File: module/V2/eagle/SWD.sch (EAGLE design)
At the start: 238 parts, among them J2 KLDX-0202-A, SW1 MF-SW-TACT-6MM, SW2 MF-SW-TACT-6MM, U1 P8X32A-Q44, U10 SN74LV4066APWR, U11 SN74LV4066APWR, U12 SN74LV4066APWR, U13 SN74LV4066APWR, U14 SN74LV4066APWR, U15 SN74LV4066APWR, U16 SN74LV4066APWR, U17 SN74LV4066APWR, U18 SN74LV4066APWR, U19 SN74LV4066APWR, U2 CAT24C512WI-GT3, U20 SN74LV4066APWR, U21 SN74LV4066APWR, U22 SN74LV4066APWR, U23 SN74LV4066APWR, U24 SSM6J507NU,LF, U25 SSM6J507NU,LF, U26 SSM6J507NU,LF, U27 SSM6J507NU,LF, U3 FT230XQ-R, U4 SN74LV4066APWR, U5 SN74LV4066APWR, U6 SN74LV4066APWR, U7 SN74LV4066APWR, U8 SN74LV4066APWR, U9 SN74LV4066APWR, X1 ABMM-6.000MHZ-B2-T

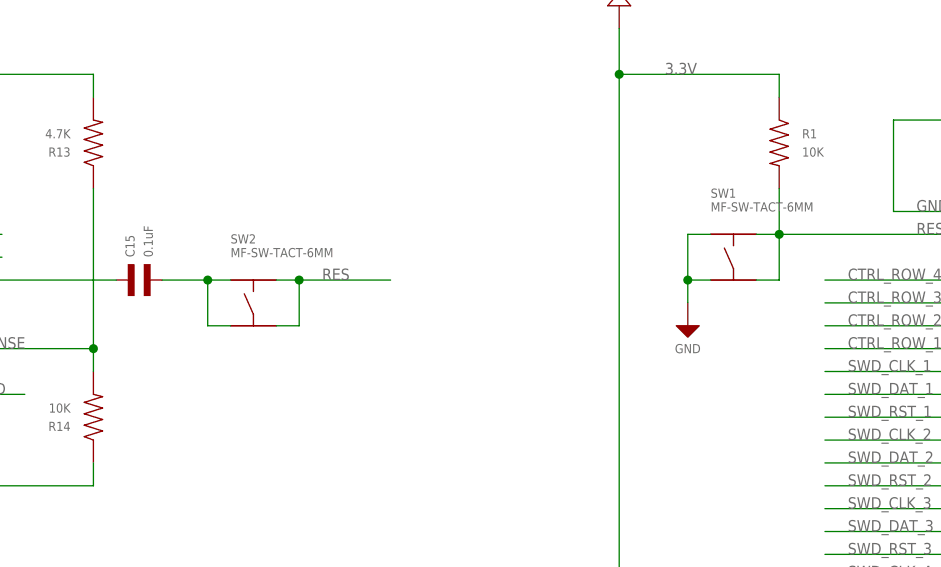
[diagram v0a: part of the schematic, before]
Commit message: Fixed wire errors
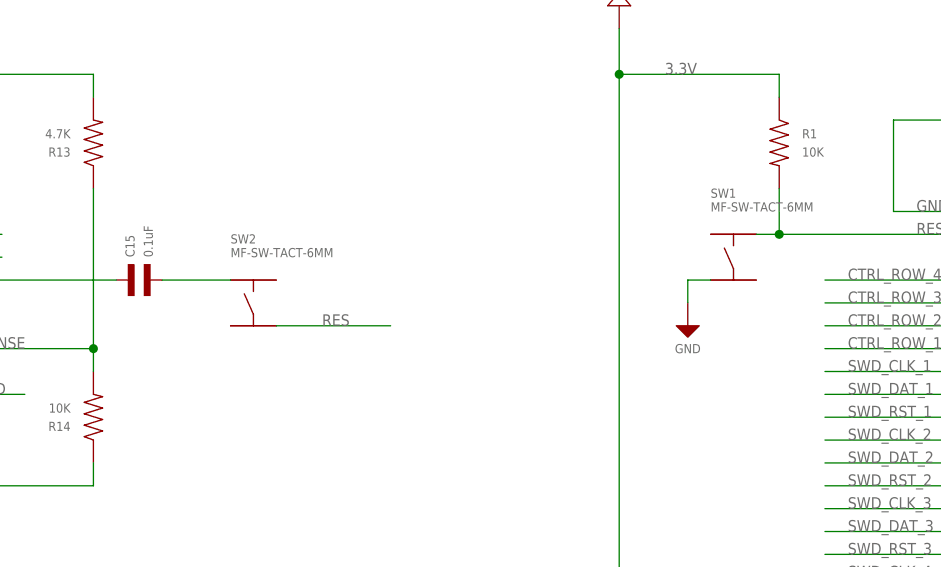
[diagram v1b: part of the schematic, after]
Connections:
- net GND: no longer SW1.P$1
- net N$18: no longer SW2.P$3
- net RES: no longer SW1.P$4, SW2.P$2
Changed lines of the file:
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@@
 <junction x="15.24" y="109.22"/>
 <label x="30.48" y="109.22" size="1.27" layer="95" font="vector"/>
-<pinref part="SW1" gate="G$1" pin="P$4"/>
-<wire x1="12.7" y1="104.14" x2="15.24" y2="104.14" width="0.1524" layer="91"/>
-<wire x1="15.24" y1="104.14" x2="15.24" y2="109.22" width="0.1524" layer="91"/>
-</segment>
-<segment>
-<pinref part="SW2" gate="G$1" pin="P$2"/>
-<wire x1="-40.64" y1="104.14" x2="-38.1" y2="104.14" width="0.1524" layer="91"/>
-<label x="-35.56" y="104.14" size="1.27" layer="95" font="vector"/>
+</segment>
+<segment>
+<label x="-35.56" y="99.06" size="1.27" layer="95" font="vector"/>
 <pinref part="SW2" gate="G$1" pin="P$4"/>
-<wire x1="-38.1" y1="104.14" x2="-27.94" y2="104.14" width="0.1524" layer="91"/>
-<wire x1="-40.64" y1="99.06" x2="-38.1" y2="99.06" width="0.1524" layer="91"/>
-<wire x1="-38.1" y1="99.06" x2="-38.1" y2="104.14" width="0.1524" layer="91"/>
-<junction x="-38.1" y="104.14"/>
+<wire x1="-40.64" y1="99.06" x2="-27.94" y2="99.06" width="0.1524" layer="91"/>
 </segment>
 </net>
@@
 <wire x1="7.62" y1="104.14" x2="5.08" y2="104.14" width="0.1524" layer="91"/>
 <wire x1="5.08" y1="104.14" x2="5.08" y2="101.6" width="0.1524" layer="91"/>
-<pinref part="SW1" gate="G$1" pin="P$1"/>
-<wire x1="7.62" y1="109.22" x2="5.08" y2="109.22" width="0.1524" layer="91"/>
-<wire x1="5.08" y1="109.22" x2="5.08" y2="104.14" width="0.1524" layer="91"/>
-<junction x="5.08" y="104.14"/>
 </segment>
 <segment>
@@
 <segment>
 <pinref part="C15" gate="G$1" pin="P$2"/>
+<wire x1="-53.34" y1="104.14" x2="-45.72" y2="104.14" width="0.1524" layer="91"/>
 <pinref part="SW2" gate="G$1" pin="P$1"/>
-<wire x1="-53.34" y1="104.14" x2="-48.26" y2="104.14" width="0.1524" layer="91"/>
-<wire x1="-48.26" y1="104.14" x2="-45.72" y2="104.14" width="0.1524" layer="91"/>
-<wire x1="-48.26" y1="104.14" x2="-48.26" y2="99.06" width="0.1524" layer="91"/>
-<pinref part="SW2" gate="G$1" pin="P$3"/>
-<wire x1="-48.26" y1="99.06" x2="-45.72" y2="99.06" width="0.1524" layer="91"/>
-<junction x="-48.26" y="104.14"/>
-</segment>
-</net>
+</segment>
+</net>
